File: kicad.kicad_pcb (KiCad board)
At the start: 2 copper layers, 100 x 70 mm, 60 parts, among them J1 Conn_01x03, J2 Screw_Terminal_01x02, J3 Conn_01x05, J4 jack3.5mm, J5 Screw_Terminal_01x02, J6 ICSP, J7 Screw_Terminal_01x03, J8 Screw_Terminal_01x03, K1 RELAY 0510, K2 RELAY 0510, Q1 BC817, Q2 BC817, SW1 SW_Push, SW2 SW_Push, T1 ZMPT101B, U1 KF33BD-TR, U2 ADS1015IDGS, U3 ESP-12E

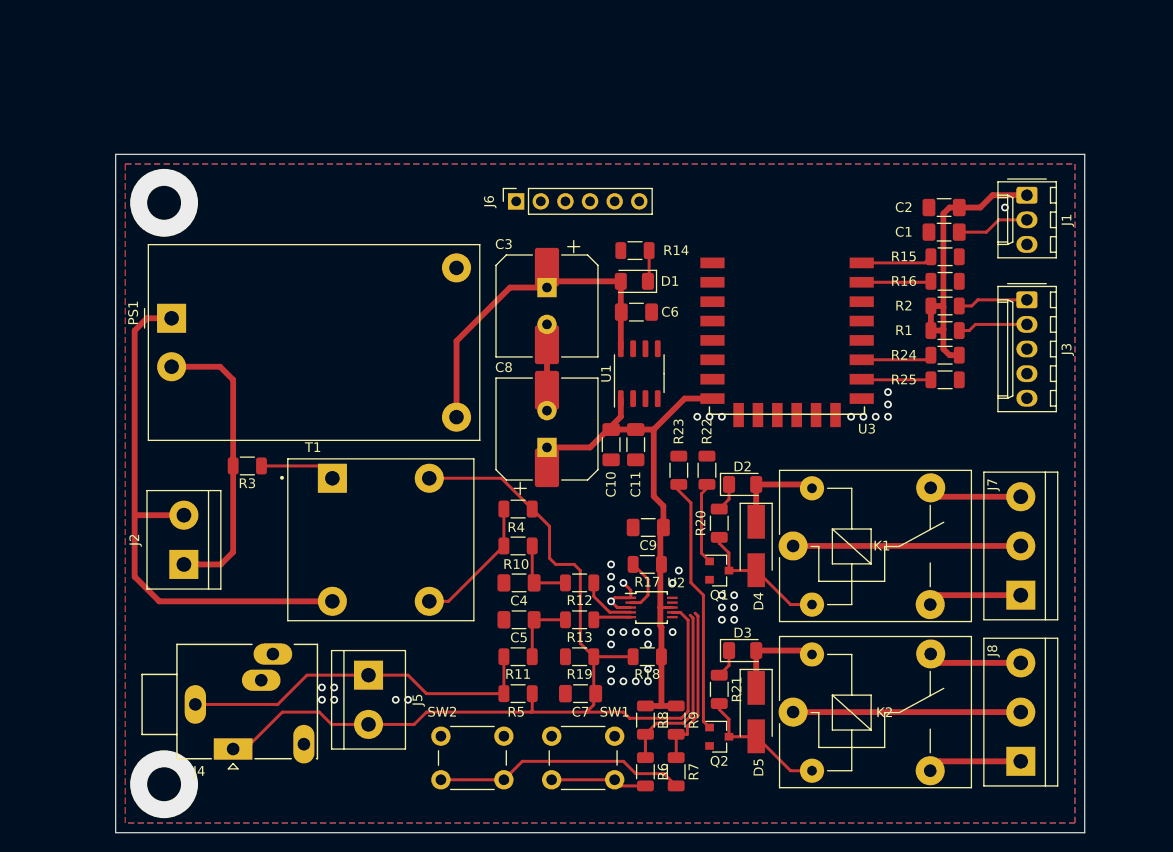
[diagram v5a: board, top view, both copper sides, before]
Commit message: mas ruteado
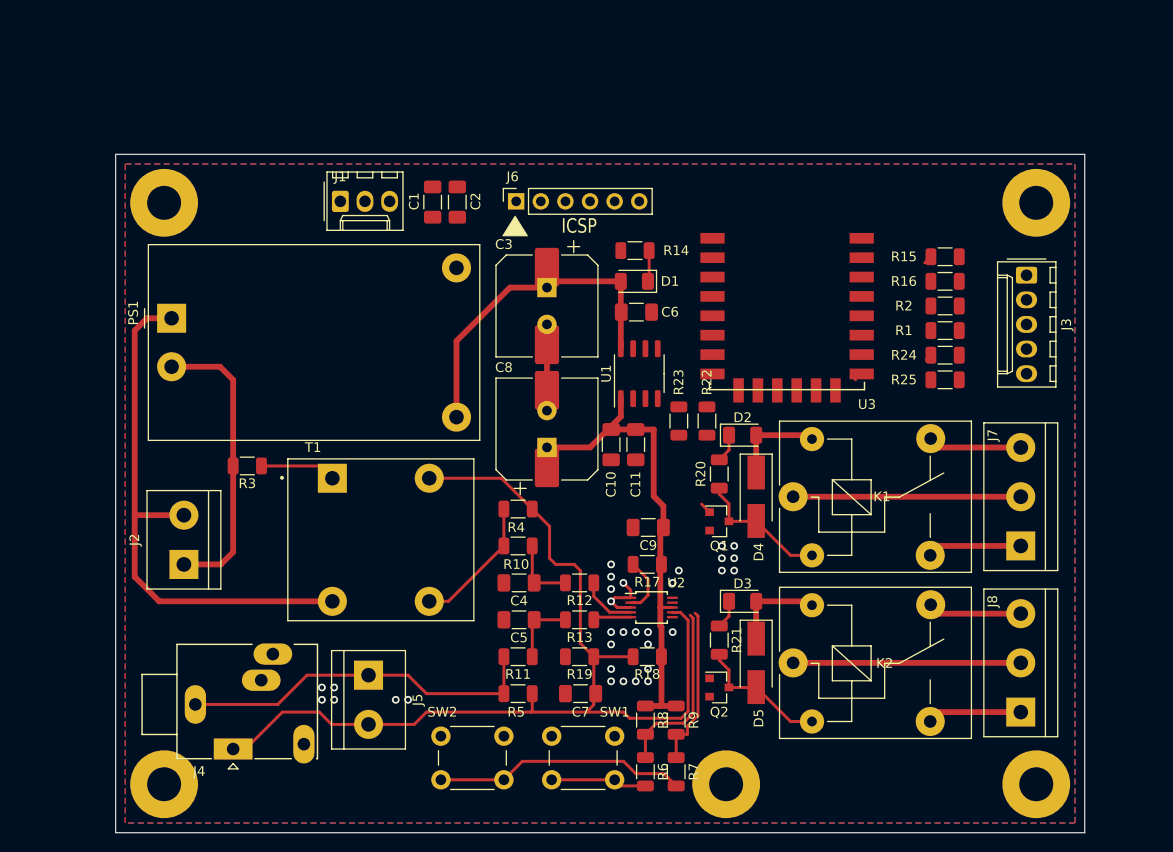
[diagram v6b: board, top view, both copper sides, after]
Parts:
- added REF**: MountingHole_3.5mm_Pad, MountingHole:MountingHole_3.5mm_Pad, F.Cu at (163.0, 130.0)
- added REF**: MountingHole_3.5mm_Pad, MountingHole:MountingHole_3.5mm_Pad, F.Cu at (195.0, 130.0)
- added REF**: MountingHole_3.5mm_Pad, MountingHole:MountingHole_3.5mm_Pad, F.Cu at (195.0, 70.0)
- added REF**: MountingHole_3.5mm_Pad, MountingHole:MountingHole_3.5mm_Pad, F.Cu at (105.0, 70.0)
- added REF**: MountingHole_3.5mm_Pad, MountingHole:MountingHole_3.5mm_Pad, F.Cu at (105.0, 130.0)
- moved J1 70.9 mm to (123.2, 69.8), turned to 0 degrees
- moved C1 52.9 mm to (132.7, 69.9), turned to 90 degrees
- moved C2 50.2 mm to (135.3, 69.9), turned to 90 degrees
- moved D5 5.08 mm to (166.1, 117.5)
- moved K2 5.08 mm to (169.9, 117.5)
- moved D2 5.08 mm to (164.7, 94.0)
- moved D3 5.08 mm to (164.7, 111.1)
- moved D4 5.08 mm to (166.1, 100.3)
- moved J7 5.08 mm to (193.4, 105.4)
- moved J8 5.08 mm to (193.4, 122.6)
- moved K1 5.08 mm to (169.9, 100.3)
- moved Q1 5.08 mm to (162.3, 102.9)
- moved Q2 5.08 mm to (162.3, 120.0)
- moved R20 5.08 mm to (162.3, 98.0)
- moved R21 5.08 mm to (162.3, 115.1)
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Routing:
- net +3V3: track 89.5 -> 50.9 mm
- net Net-(Q2-Pad1): track 26.1 -> 0.00 mm
- net Net-(R25-Pad1): track 7.87 -> 0.00 mm
- net RXD0: track 7.88 -> 0.13 mm
- net TEMP: track 7.51 -> 0.00 mm
- net Net-(R24-Pad2): track 8.04 -> 0.67 mm
- net SDA: track 7.25 -> 0.00 mm
- net SCL: track 7.25 -> 0.00 mm
- net TXD0: track 8.10 -> 0.90 mm
- net Net-(Q1-Pad1): track 8.13 -> 1.18 mm
- net GND: track 15.2 -> 15.3 mm, vias 44 -> 32
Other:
- board text added: "ICSP"

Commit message: terminado ruteado principal
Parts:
- moved J4 6.30 mm to (106.4, 123.8)
- moved J5 6.21 mm to (120.0, 117.5)
- moved R22 5.67 mm to (159.5, 98.0)
- moved R23 5.58 mm to (157.0, 98.0)
- moved REF** 2.00 mm to (165.0, 130.0)
- moved J3 1.99 mm to (192.0, 77.7)
- moved J6 1.27 mm to (140.1, 69.8)
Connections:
- PS1 pad 1: Net-(J2-Pad2) -> Net-(J2-Pad1)
- PS1 pad 2: Net-(J2-Pad1) -> Net-(J2-Pad2)
- R3 pad 2: Net-(J2-Pad1) -> Net-(J2-Pad2)
- T1 pad 2: Net-(J2-Pad2) -> Net-(J2-Pad1)
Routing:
- net +3V3: track 50.9 -> 189.4 mm, vias 0 -> 1
- net +5V: track 56.0 -> 150.6 mm, vias 0 -> 8
- net GPIO0: track 16.6 -> 108.1 mm, vias 0 -> 2
- net RESET: track 18.5 -> 95.2 mm, vias 0 -> 2
- net SCL: track 0.00 -> 68.9 mm, vias 0 -> 3
- net SDA: track 0.00 -> 68.4 mm, vias 0 -> 3
- net Net-(J6-Pad2): track 0.00 -> 55.1 mm, vias 0 -> 1
- net Net-(J6-Pad3): track 0.00 -> 53.4 mm, vias 0 -> 1
- net TEMP: track 0.00 -> 41.8 mm, vias 0 -> 2
- net Net-(J2-Pad2): track 56.3 -> 24.3 mm
- net RDY: track 5.92 -> 35.0 mm, vias 0 -> 2
- net Net-(J8-Pad2): track 23.5 -> 47.0 mm
- net Net-(J7-Pad2): track 23.5 -> 47.0 mm
- net Net-(Q2-Pad1): track 0.00 -> 21.4 mm
- net RELAY_1: track 0.00 -> 20.4 mm, vias 0 -> 2
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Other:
- outline, holes or cut-outs redrawn
- board text added: "3V3"
- board text added: "5V0"
- board text added: "BOOT"
- board text added: "Design By E.W. Philippeaux"
- board text added: "GND"
- board text added: "IO0"
- board text added: "PowerMike"
- board text added: "RESET"
- board text added: "RST"
- board text added: "RXD"
- board text added: "SCL"
- board text added: "SDA"
- board text added: "TXD"
- board text added: "https://bit.ly/3ayiguX"
